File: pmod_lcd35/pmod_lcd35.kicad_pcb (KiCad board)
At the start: 2 copper layers, 65 x 75 mm, 21 parts, among them J1 PMOD_0, J2 PMOD_1, U1 TPS61165

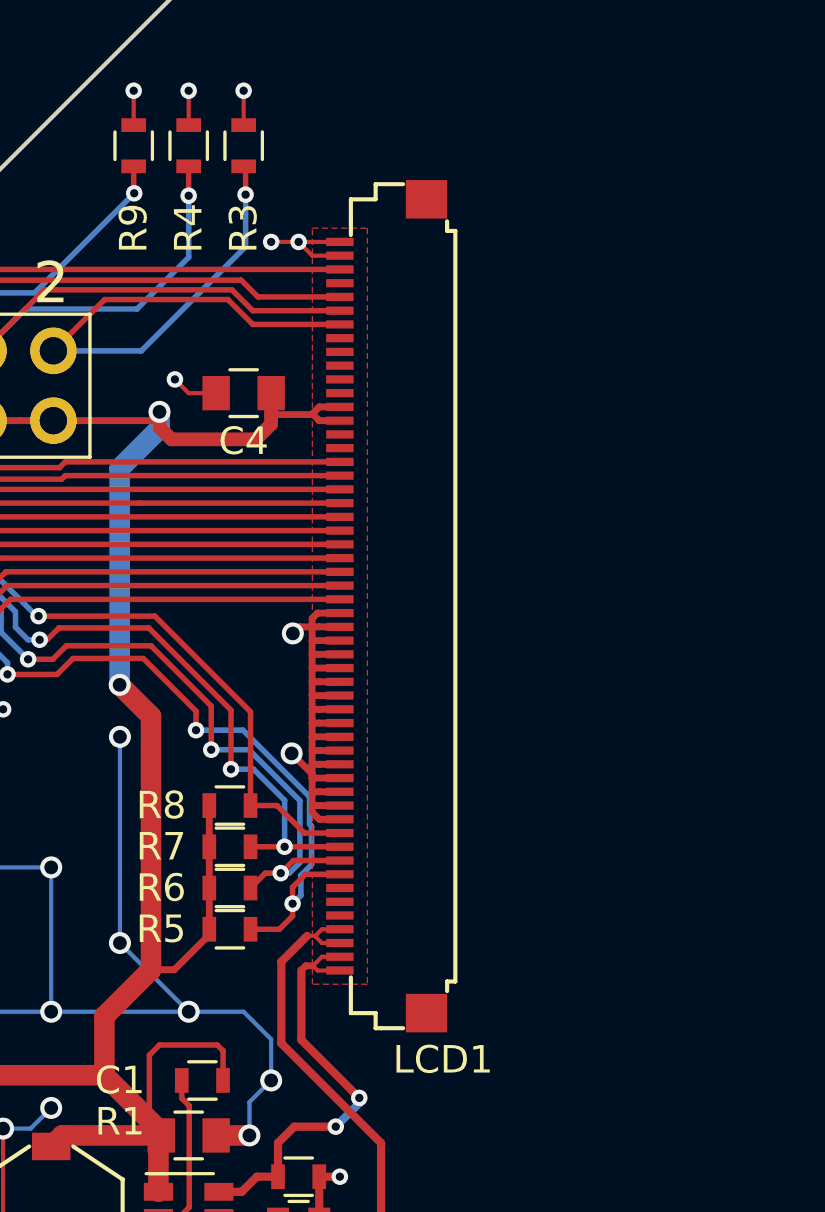
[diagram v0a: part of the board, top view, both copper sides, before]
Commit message: Change FFC footprint
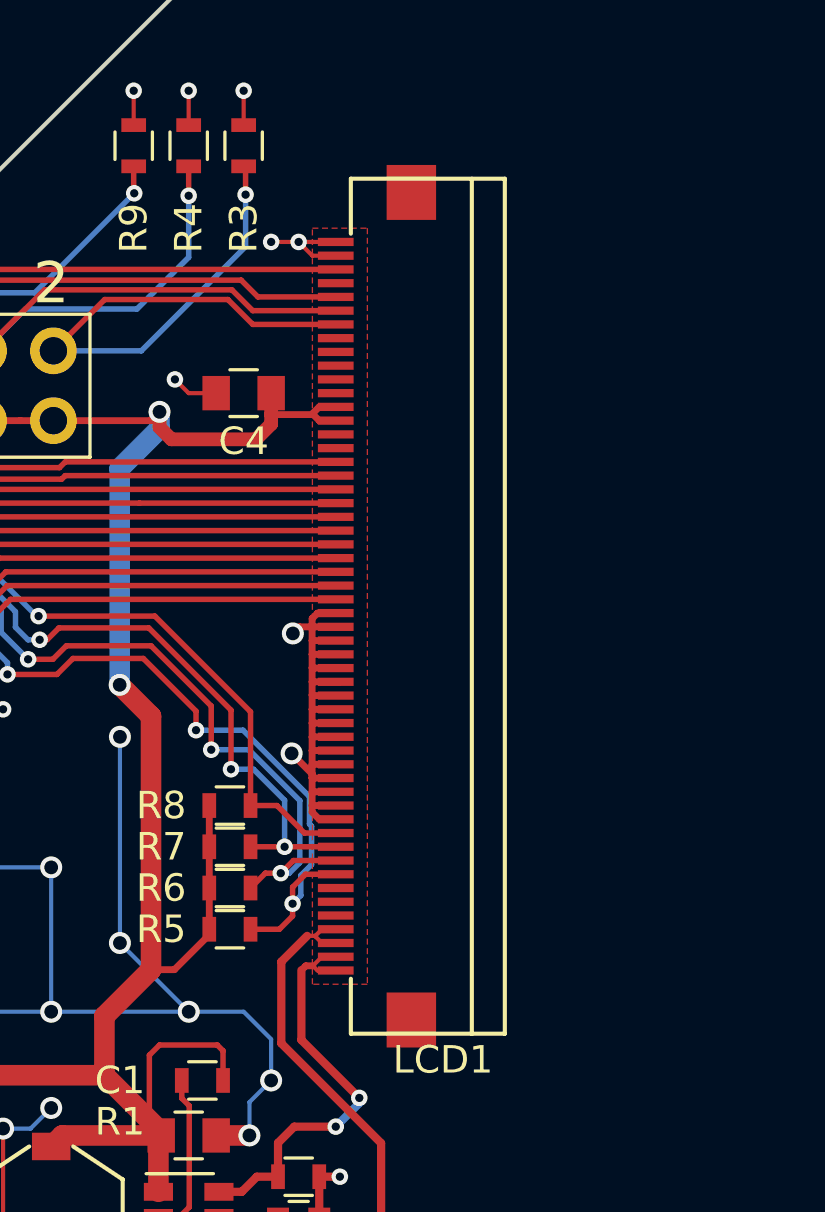
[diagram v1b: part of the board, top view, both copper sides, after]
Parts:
- LCD1: footprint Custom Parts:MOLEX_51296-5494_54pin_0.5mm_BTM -> Custom Parts:CviLux_CF25541D0R0-05-NH
